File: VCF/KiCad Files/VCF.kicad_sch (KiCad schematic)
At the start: 64 parts, among them J1 CV1, J2 CV2, J3 AUDIO_IN, J4 AUDIO_OUT, J5 Conn_02x05_Odd_Even, J6 Conn_01x05_Male, J7 Conn_01x05_Female, J8 Conn_01x08_Male, J9 Conn_01x08_Female, SW1 SW_DPDT_x2, U1 TL074, U2 TL074

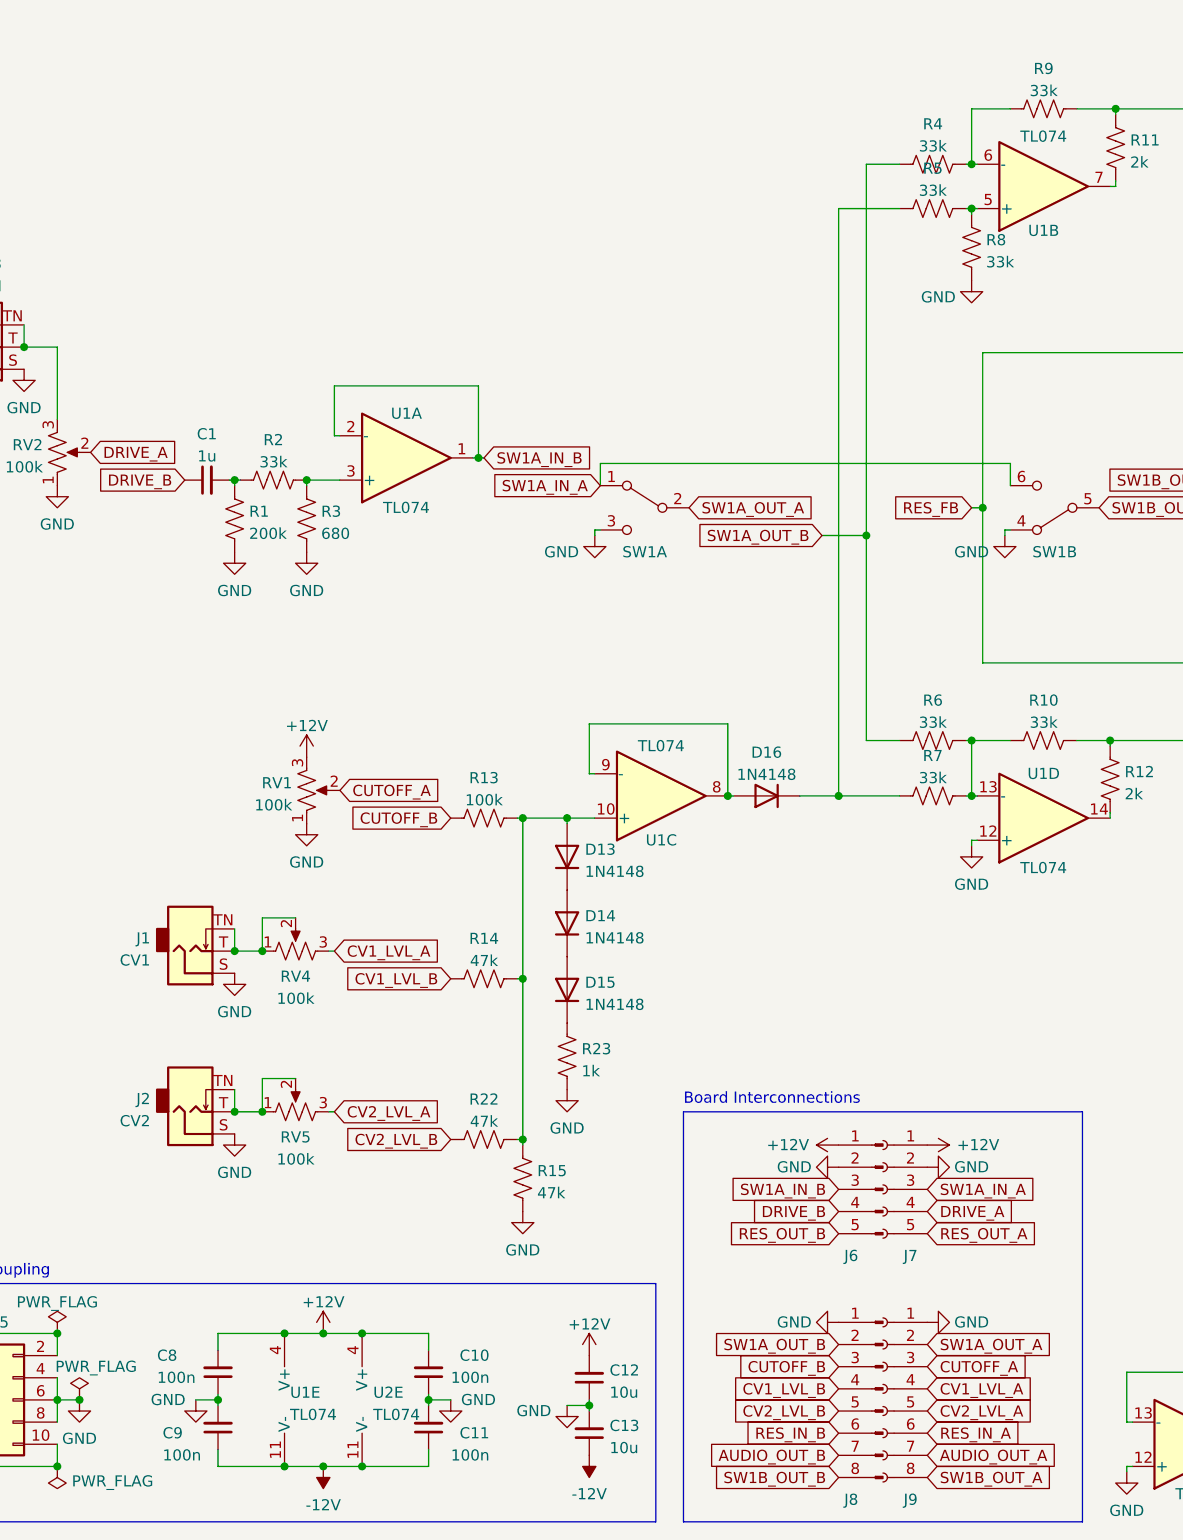
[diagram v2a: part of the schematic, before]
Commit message: Added PDF schematic
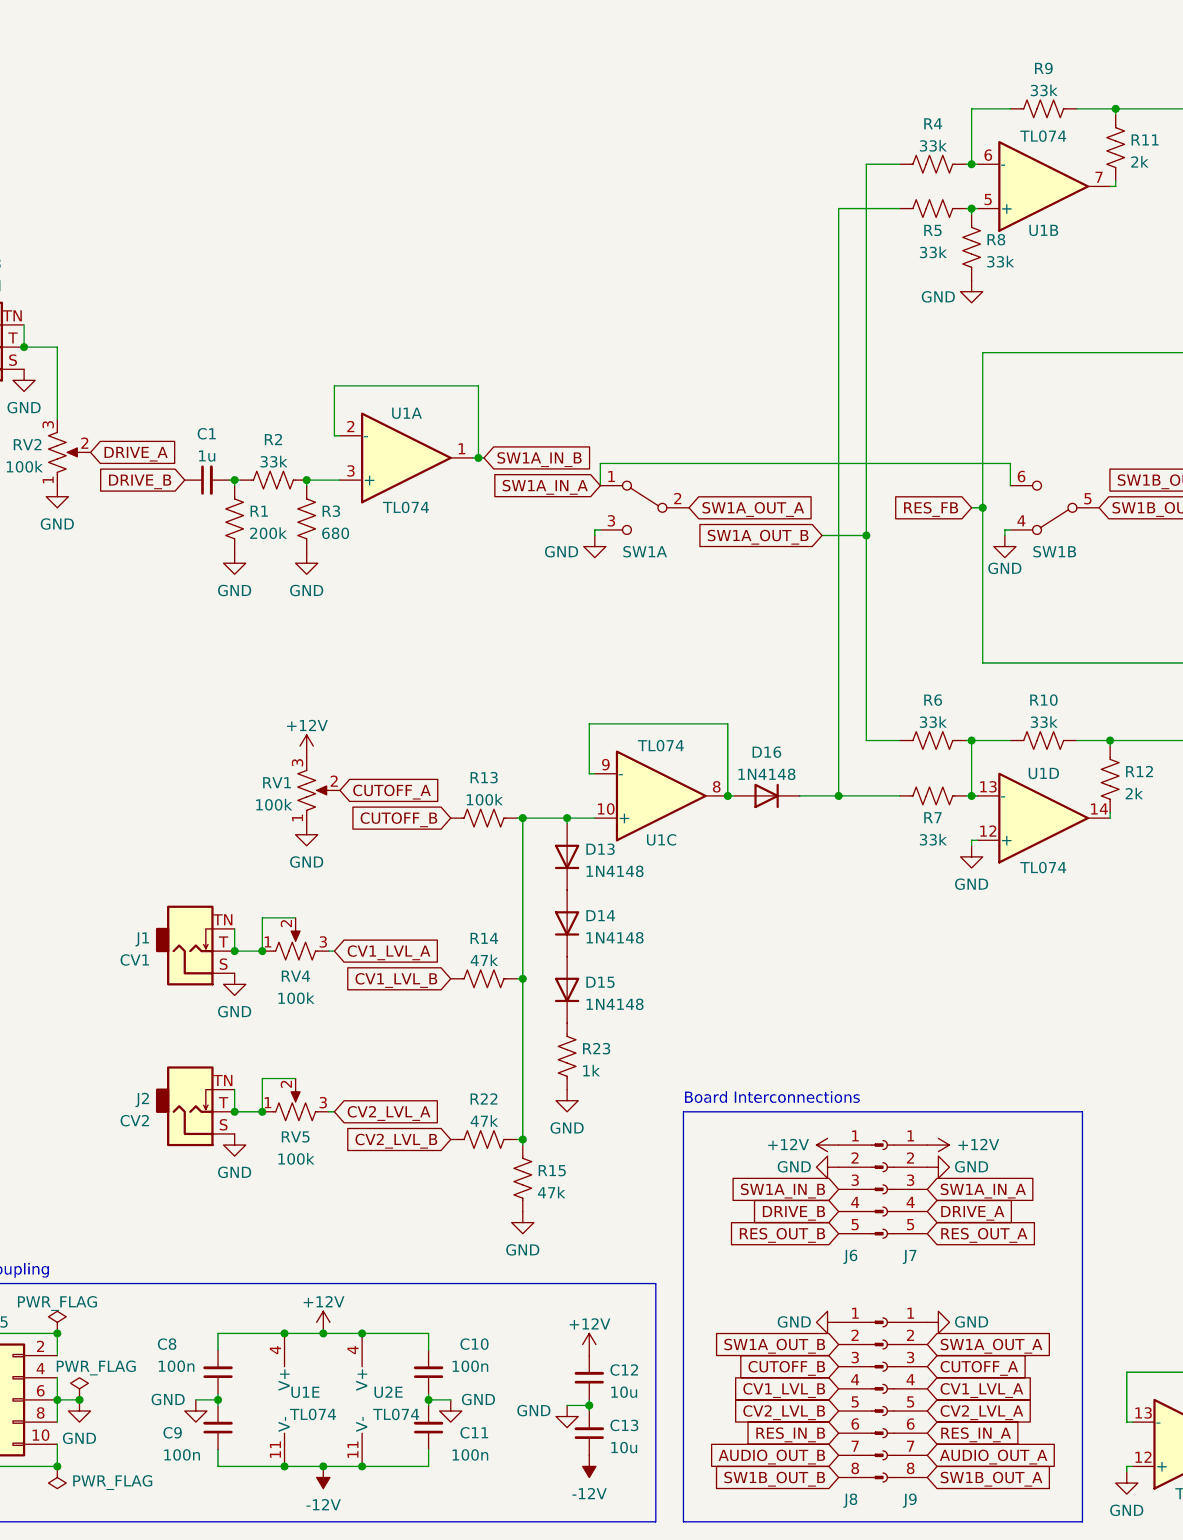
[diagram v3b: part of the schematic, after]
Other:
- company: Drachma Mfg -> (none)
- title: Moritz Klein Diode Ladder VCF -> Moritz Klein Diode-Ladder VCF
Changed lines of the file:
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@@
   (paper "A4")
   (title_block
-    (title "Moritz Klein Diode Ladder VCF")
+    (title "Moritz Klein Diode-Ladder VCF")
     (rev "1")
-    (company "Drachma Mfg")
   )
   (junction (at 55.245 149.86) (diameter 0) (color 0 0 0 0)
@@
   )
   (symbol (lib_id "Device:R_US") (at 132.08 46.355 90) (unit 1)
-    (in_bom yes) (on_board yes) (fields_autoplaced)
-    (property "Reference" "R5" (id 0) (at 132.08 41.7662 90))
-    (property "Value" "33k" (id 1) (at 132.08 44.3031 90))
+    (in_bom yes) (on_board yes)
+    (property "Reference" "R5" (id 0) (at 132.08 48.8981 90))
+    (property "Value" "33k" (id 1) (at 132.08 51.435 90))
     (property "Footprint" "Resistor_SMD:R_0603_1608Metric_Pad0.98x0.95mm_HandSolder" (id 2) (at 132.334 45.339 90)
       (effects (font (size 1.27 1.27)) hide)
@@
   (symbol (lib_id "Device:C_Small") (at 74.295 179.705 0) (mirror x) (unit 1)
     (in_bom yes) (on_board yes)
-    (property "Reference" "C10" (id 0) (at 81.28 177.8 0)
-      (effects (font (size 1.27 1.27)) (justify right))
-    )
-    (property "Value" "100n" (id 1) (at 81.28 180.3369 0)
+    (property "Reference" "C10" (id 0) (at 81.28 176.5331 0)
+      (effects (font (size 1.27 1.27)) (justify right))
+    )
+    (property "Value" "100n" (id 1) (at 81.28 179.07 0)
       (effects (font (size 1.27 1.27)) (justify right))
     )
@@
   (symbol (lib_id "Device:C_Small") (at 50.165 179.705 180) (unit 1)
     (in_bom yes) (on_board yes)
-    (property "Reference" "C8" (id 0) (at 43.18 177.8 0)
-      (effects (font (size 1.27 1.27)) (justify right))
-    )
-    (property "Value" "100n" (id 1) (at 43.18 180.3369 0)
+    (property "Reference" "C8" (id 0) (at 43.18 176.53 0)
+      (effects (font (size 1.27 1.27)) (justify right))
+    )
+    (property "Value" "100n" (id 1) (at 43.18 179.0669 0)
       (effects (font (size 1.27 1.27)) (justify right))
     )
@@
       (effects (font (size 1.27 1.27)) hide)
     )
-    (property "Value" "GND" (id 1) (at 136.525 85.725 0))
+    (property "Value" "GND" (id 1) (at 140.335 87.63 0))
     (property "Footprint" "" (id 2) (at 140.335 83.82 0)
       (effects (font (size 1.27 1.27)) hide)
@@
   )
   (symbol (lib_id "Device:R_US") (at 132.08 113.665 90) (unit 1)
-    (in_bom yes) (on_board yes) (fields_autoplaced)
-    (property "Reference" "R7" (id 0) (at 132.08 109.0762 90))
-    (property "Value" "33k" (id 1) (at 132.08 111.6131 90))
+    (in_bom yes) (on_board yes)
+    (property "Reference" "R7" (id 0) (at 132.08 116.205 90))
+    (property "Value" "33k" (id 1) (at 132.08 118.7419 90))
     (property "Footprint" "Resistor_SMD:R_0603_1608Metric_Pad0.98x0.95mm_HandSolder" (id 2) (at 132.334 112.649 90)
       (effects (font (size 1.27 1.27)) hide)

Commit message: Added BOM
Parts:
- C1, C7: footprint Capacitor_SMD:C_0603_1608Metric_Pad1.08x0.95mm_HandSolder -> Capacitor_SMD:C_1206_3216Metric_Pad1.33x1.80mm_HandSolder
- C10, C11, C8, C9: footprint Capacitor_SMD:C_0603_1608Metric_Pad1.08x0.95mm_HandSolder -> Capacitor_SMD:C_0805_2012Metric_Pad1.18x1.45mm_HandSolder
- R1, R10, R11, R12, R13, R14, R15, R16, R17, R18, R19, R2, R20, R22, R23, R3, R4, R5, R6, R7, R8, R9: footprint Resistor_SMD:R_0603_1608Metric_Pad0.98x0.95mm_HandSolder -> Resistor_SMD:R_0805_2012Metric_Pad1.20x1.40mm_HandSolder

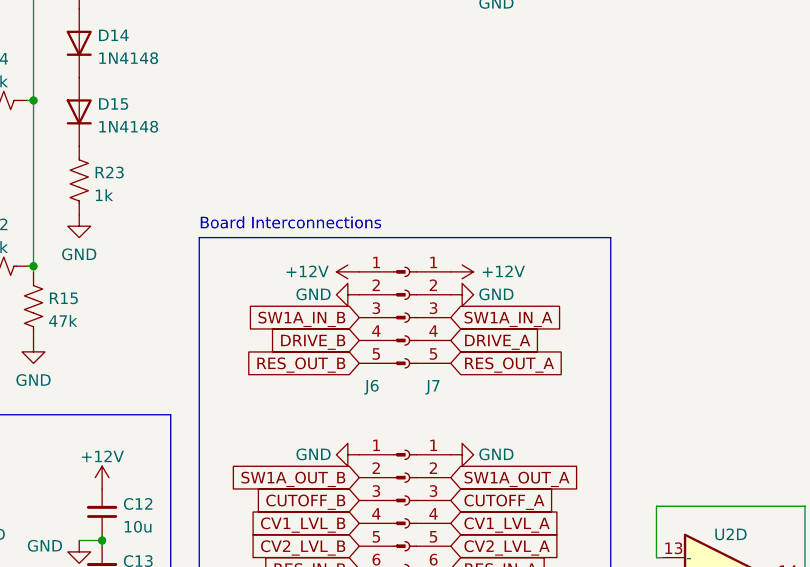
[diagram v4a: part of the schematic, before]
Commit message: Corrected footprints
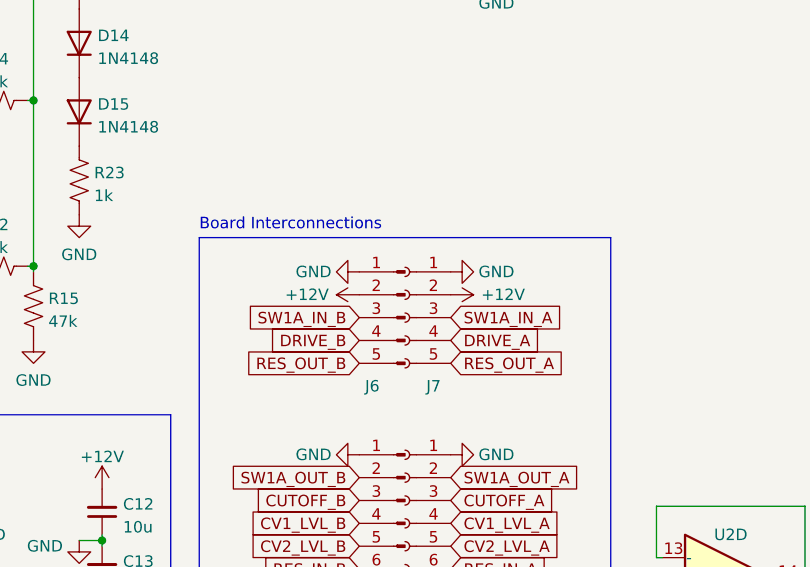
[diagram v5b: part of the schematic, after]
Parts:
- C1, C7: footprint Capacitor_SMD:C_1206_3216Metric_Pad1.33x1.80mm_HandSolder -> Capacitor_THT:C_Rect_L7.2mm_W3.5mm_P5.00mm_FKS2_FKP2_MKS2_MKP2
- C10, C11, C8, C9: footprint Capacitor_SMD:C_0805_2012Metric_Pad1.18x1.45mm_HandSolder -> Capacitor_THT:C_Disc_D3.8mm_W2.6mm_P2.50mm
- C12, C13: footprint Capacitor_SMD:CP_Elec_5x5.4 -> Capacitor_THT:CP_Radial_D5.0mm_P2.00mm
- C2, C3, C4, C5, C6: footprint Capacitor_SMD:C_0603_1608Metric_Pad1.08x0.95mm_HandSolder -> Capacitor_THT:C_Rect_L7.2mm_W2.5mm_P5.00mm_FKS2_FKP2_MKS2_MKP2
- D1, D13, D14, D15, D16, D2, D3, D4, D5, D6, D7, D8: footprint Diode_SMD:D_SOD-323_HandSoldering -> Diode_THT:D_DO-35_SOD27_P7.62mm_Horizontal
- R1, R10, R11, R12, R13, R14, R15, R16, R17, R18, R19, R2, R20, R22, R23, R3, R4, R5, R6, R7, R8, R9: footprint Resistor_SMD:R_0805_2012Metric_Pad1.20x1.40mm_HandSolder -> Resistor_THT:R_Axial_DIN0207_L6.3mm_D2.5mm_P7.62mm_Horizontal
- U1, U2: footprint Package_SO:SOIC-14_3.9x8.7mm_P1.27mm -> Package_DIP:DIP-14_W7.62mm
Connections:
- net +12V: now also J6.2 (Pin_2), J7.2 (Pin_2); no longer J6.1 (Pin_1), J7.1 (Pin_1)
- net GND: now also J6.1 (Pin_1), J7.1 (Pin_1); no longer J6.2 (Pin_2), J7.2 (Pin_2)
